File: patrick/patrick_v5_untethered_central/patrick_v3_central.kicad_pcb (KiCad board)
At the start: 2 copper layers, 53.1 x 53.9 mm, 24 parts, among them IC1 IS32FL3237-TQLA3, J1 Conn_02x05_Counter_Clockwise, J10 61300311121, J2 Conn_02x05_Counter_Clockwise, J3 Conn_02x05_Counter_Clockwise, J4 Conn_02x05_Counter_Clockwise, J5 Conn_02x05_Counter_Clockwise, J6 DM3CS-SF, J7 61300211121, J8 Conn_01x03, U1 ICM-20948, U2 MCP1702T-1802E_CB, U3 BL652-SA-01

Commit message: imu change
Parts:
- added Q1: RUE002N02TL, RUE002N02TL:TRANS_RUE002N02TL, B.Cu at (124.6, 109.1)
- added Q2: RUE002N02TL, RUE002N02TL:TRANS_RUE002N02TL, F.Cu at (115.9, 113.2)
- added Q3: RUE002N02TL, RUE002N02TL:TRANS_RUE002N02TL, F.Cu at (117.4, 107.2)
- added R5: , Resistor_SMD:R_0402_1005Metric, B.Cu at (122.9, 109.1)
- added R6: , Resistor_SMD:R_0402_1005Metric, F.Cu at (115.9, 111.4)
- added R7: , Resistor_SMD:R_0402_1005Metric, F.Cu at (117.5, 108.8)
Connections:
- U1 pad 12: Net-(U1-Pad12) -> /INT_VIN
- U1 pad 23: /SCL -> /SCL_VIN
- U1 pad 24: /SDA -> /SDA_VIN
- U3 pad 2: Net-(U1-Pad12) -> /INT
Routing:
- net +1V8: track 28.5 -> 58.2 mm, vias 0 -> 1
- net /SDA_VIN: track 0.00 -> 10.9 mm, vias 0 -> 1
- net /SDA: track 222.3 -> 215.7 mm, vias 12 -> 13
- net Net-(U1-Pad12): track 5.79 -> 0.00 mm, vias 1 -> 0
- net /INT: track 0.00 -> 4.85 mm
- net /INT_VIN: track 0.00 -> 4.30 mm, vias 0 -> 1
- net /SCL_VIN: track 0.00 -> 2.90 mm
- net /SMA11_SIG: track 19.8 -> 22.4 mm
- net /SMA12_SIG: track 19.8 -> 22.3 mm
- net /SCL: track 221.9 -> 220.4 mm, vias 12 -> 13
- net GND: track 302.0 -> 302.8 mm

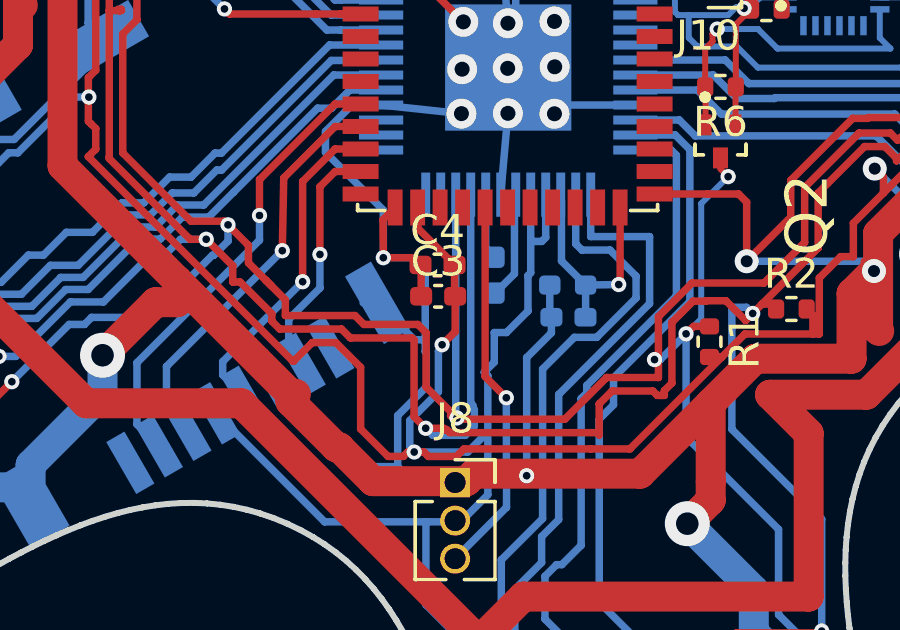
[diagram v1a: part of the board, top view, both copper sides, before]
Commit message: LED switcher useless
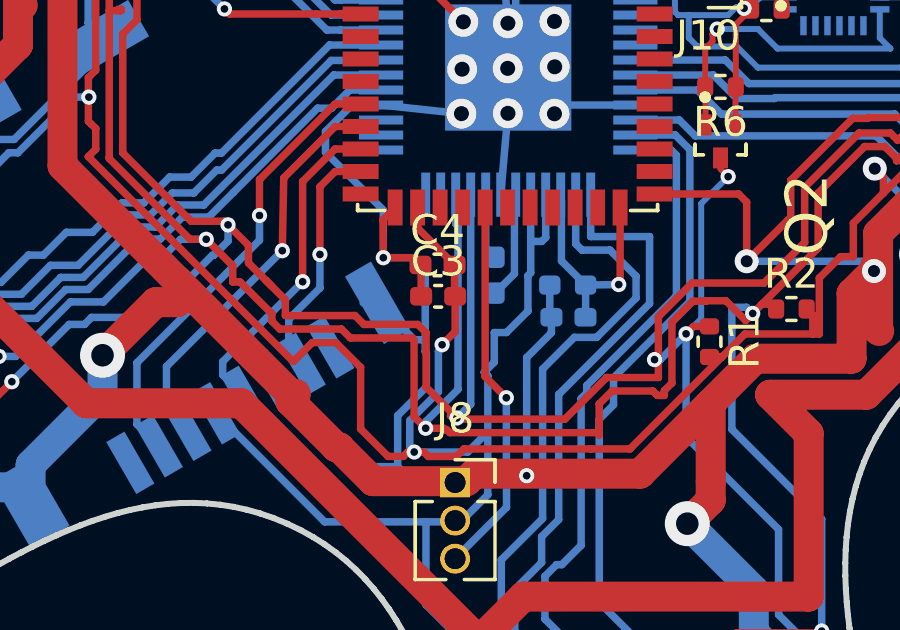
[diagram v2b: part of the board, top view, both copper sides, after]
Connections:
- IC1 pad 45: /SCL -> /SDA
- IC1 pad 46: /SDA -> /SCL
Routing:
- net /SCL: track 220.4 -> 219.0 mm
